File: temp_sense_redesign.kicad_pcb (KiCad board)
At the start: 2 copper layers, 102.4 x 43 mm, 100 parts, among them IC1 TPS7A03, IC2 LM74500QDDFRQ1, J1 Screw_Terminal_01x08, J2 Screw_Terminal_01x08, J3 Screw_Terminal_01x08, J4 Conn_01x02_Pin, J5 Screw_Terminal_01x02, J6 Screw_Terminal_01x08, J7 Conn_01x02_Pin, J8 Screw_Terminal_01x02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

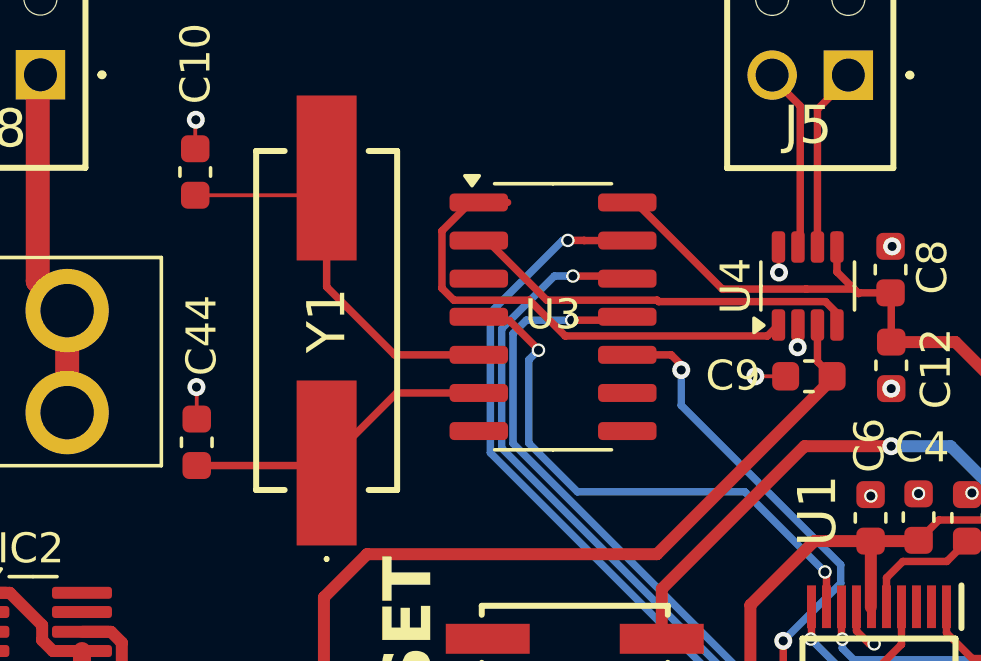
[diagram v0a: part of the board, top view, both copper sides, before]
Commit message: Add KiCad .gitignore, remove gerber/backup/cache files from tracking
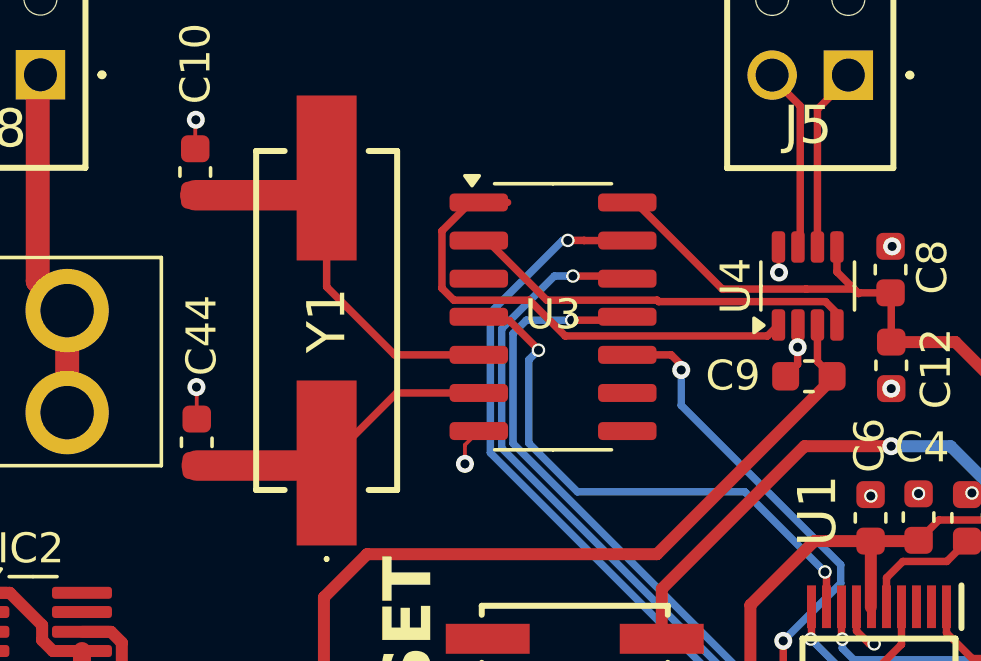
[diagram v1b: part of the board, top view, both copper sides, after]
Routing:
- net GND: track 36.3 -> 37.7 mm
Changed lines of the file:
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@@
 			(plot_on_all_layers_selection 0x00000000_00000000_00000000_00000000)
 			(disableapertmacros no)
-			(usegerberextensions no)
+			(usegerberextensions yes)
 			(usegerberattributes yes)
 			(usegerberadvancedattributes yes)
@@
 			(outputformat 1)
 			(mirror no)
-			(drillshape 1)
+			(drillshape 0)
 			(scaleselection 1)
-			(outputdirectory "")
+			(outputdirectory "gerber/")
 		)
 	)
@@
 		(start 111.39 68.555)
 		(end 115.635 68.555)
-		(width 0.25)
+		(width 1.016)
 		(layer "F.Cu")
 		(net "Net-(U3-OSC1)")
@@
 		(start 111.34 59.545)
 		(end 115.145 59.545)
-		(width 0.127)
+		(width 1.016)
 		(layer "F.Cu")
 		(net "Net-(U3-OSC2)")
@@
 	)
 	(segment
-		(start 155.87 84.24)
-		(end 155.87 85.13)
-		(width 0.127)
+		(start 131.42 65.18)
+		(end 131.02 65.58)
+		(width 0.25)
 		(layer "F.Cu")
 		(net "GND")
 	)
 	(segment
-		(start 131.02 65.58)
-		(end 130.01 65.58)
+		(start 155.87 84.24)
+		(end 155.87 85.13)
 		(width 0.127)
 		(layer "F.Cu")
@@
 	)
 	(segment
+		(start 120.79175 67.40575)
+		(end 120.33 67.8675)
+		(width 0.127)
+		(layer "F.Cu")
+		(net "GND")
+	)
+	(segment
 		(start 146.96 67.34)
 		(end 146.96 66.3)
@@
 	)
 	(segment
+		(start 120.33 67.8675)
+		(end 120.33 68.5)
+		(width 0.127)
+		(layer "F.Cu")
+		(net "GND")
+	)
+	(segment
 		(start 172.83 66.25)
 		(end 172.82 66.24)
@@
 		(net "GND")
 	)
+	(segment
+		(start 131.42 64.61)
+		(end 131.42 65.18)
+		(width 0.25)
+		(layer "F.Cu")
+		(net "GND")
+	)
 	(via
 		(at 159.93 66.23)
@@
 	)
 	(via
-		(at 130.01 65.58)
+		(at 120.33 68.5)
 		(size 0.6)
 		(drill 0.3)
 		(layers "F.Cu" "B.Cu")
-		(capping no)
-		(covering
-			(front no)
-			(back no)
-		)
-		(plugging
-			(front no)
-			(back no)
-		)
-		(filling no)
 		(net "GND")
 	)
